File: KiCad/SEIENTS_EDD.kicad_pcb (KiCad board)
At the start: 2 copper layers, 130.1 x 90 mm, 99 parts, among them IC1 A3144EUA, J1 Conn_01x02_Pin, J201 Screw_Terminal_01x04, J3 Screw_Terminal_01x05, J4 Screw_Terminal_01x02, J7 DE9_Socket, J8 DE9_Pins, M4 Motor_DC, M5 Motor_DC, M6 Motor_DC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

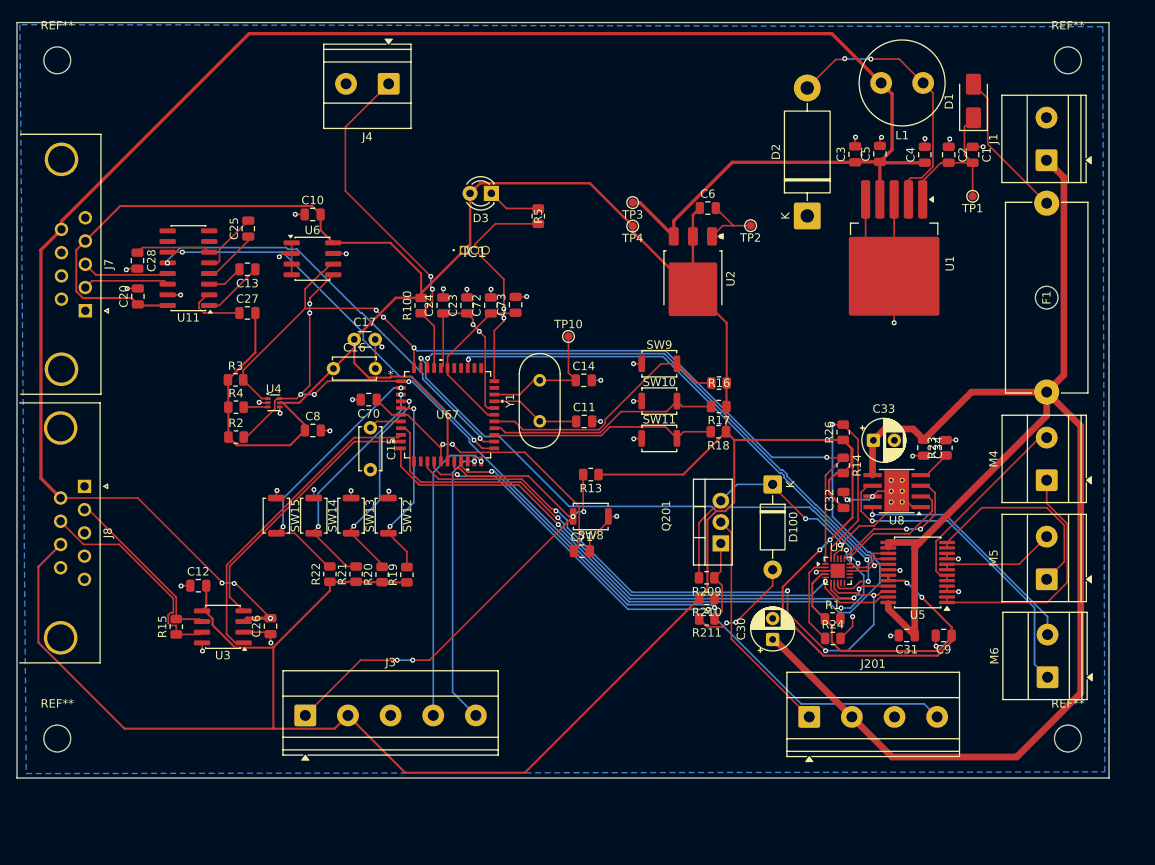
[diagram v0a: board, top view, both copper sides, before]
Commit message: Afegit el LTSpice
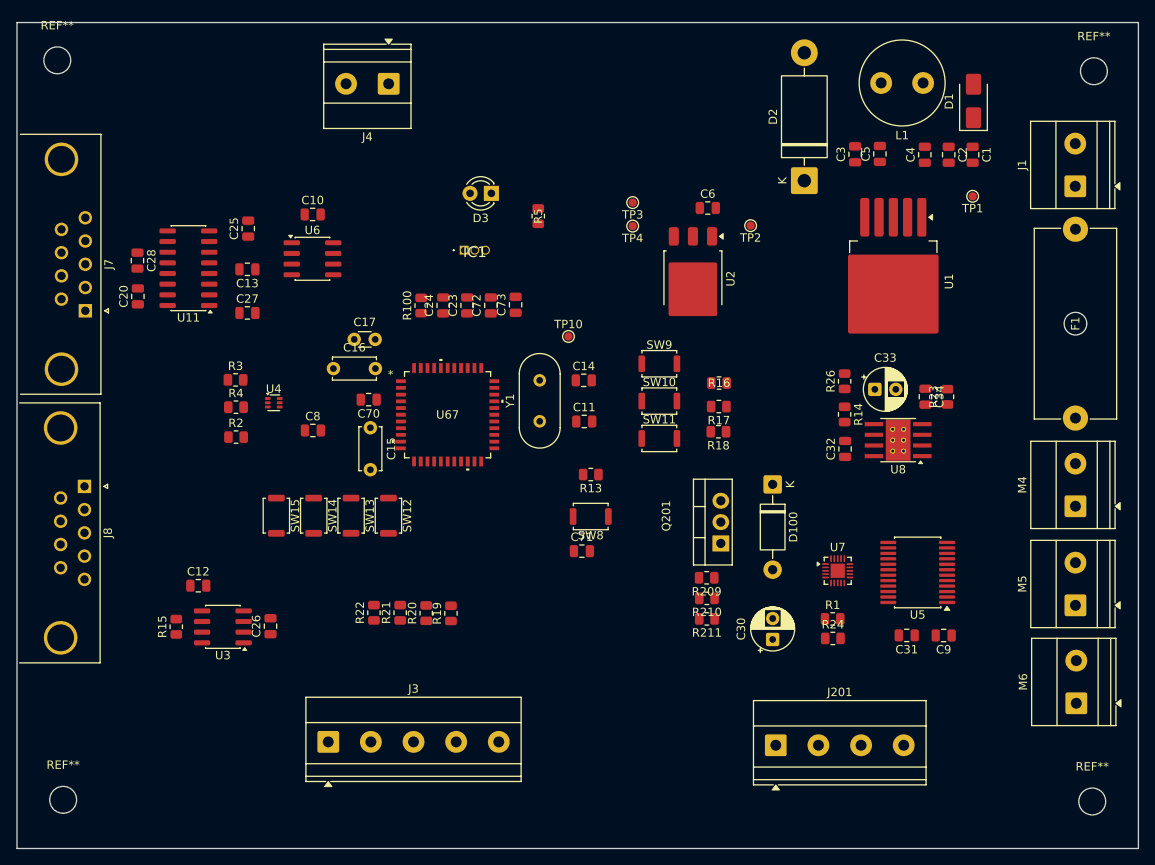
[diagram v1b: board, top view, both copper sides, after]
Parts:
- moved REF** 8.04 mm to (218.0, 147.8)
- moved REF** 7.33 mm to (95.4, 147.6)
- moved R19 6.98 mm to (141.6, 125.4)
- moved R22 6.98 mm to (132.4, 125.3)
- moved R20 6.98 mm to (138.7, 125.4)
- moved R21 6.98 mm to (135.6, 125.3)
- moved C32 6.08 mm to (188.6, 105.8)
- moved C34 6.08 mm to (198.1, 99.6)
- moved R14 6.08 mm to (188.5, 101.7)
- moved R26 6.08 mm to (188.5, 97.7)
- moved U8 6.08 mm to (194.9, 104.8)
- moved C33 6.08 mm to (192.1, 98.7)
- moved R23 6.08 mm to (200.8, 99.6)
- moved J201 5.22 mm to (180.3, 141.1)
- moved M5 4.62 mm to (216.0, 124.4)
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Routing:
- net +3.3V: track 519.9 -> 0.00 mm, vias 4 -> 0
- net +5V: track 235.2 -> 0.00 mm, vias 3 -> 0
- net VBAT: track 185.8 -> 0.00 mm
- net GND: track 153.2 -> 0.00 mm, vias 48 -> 0
- net MCU_SDA: track 148.8 -> 0.00 mm, vias 6 -> 0
- net MCU_SCL: track 109.7 -> 0.00 mm, vias 4 -> 0
- net POS_IN2: track 77.6 -> 0.00 mm, vias 4 -> 0
- net POS_PWM: track 72.3 -> 0.00 mm, vias 2 -> 0
- net POS_IN1: track 72.1 -> 0.00 mm, vias 3 -> 0
- net T_SEIENTS: track 71.5 -> 0.00 mm, vias 2 -> 0
- net REC_IN2: track 71.0 -> 0.00 mm, vias 2 -> 0
- net REC_IN1: track 70.5 -> 0.00 mm, vias 2 -> 0
- net REC_PWM: track 69.1 -> 0.00 mm, vias 3 -> 0
- net Net-(J3-Pin_1): track 65.0 -> 0.00 mm, vias 4 -> 0
- net CALEFACCIÓ: track 51.9 -> 0.00 mm, vias 2 -> 0
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- removed copper zone on B.Cu, net GND
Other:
- board size 130.1 x 90 mm -> 133.6 x 98.4 mm

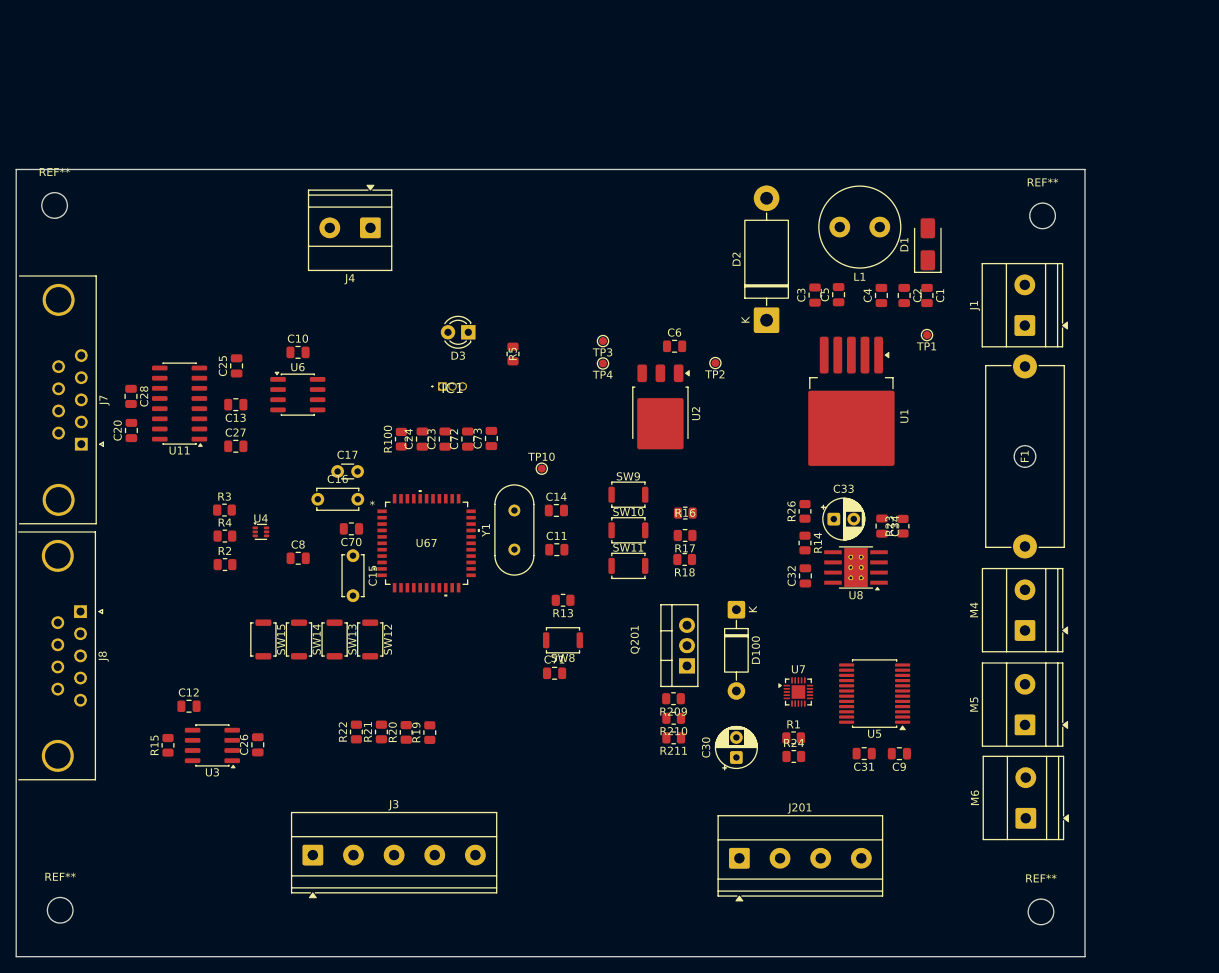
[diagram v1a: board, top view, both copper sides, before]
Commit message: Afegit el LTSpice
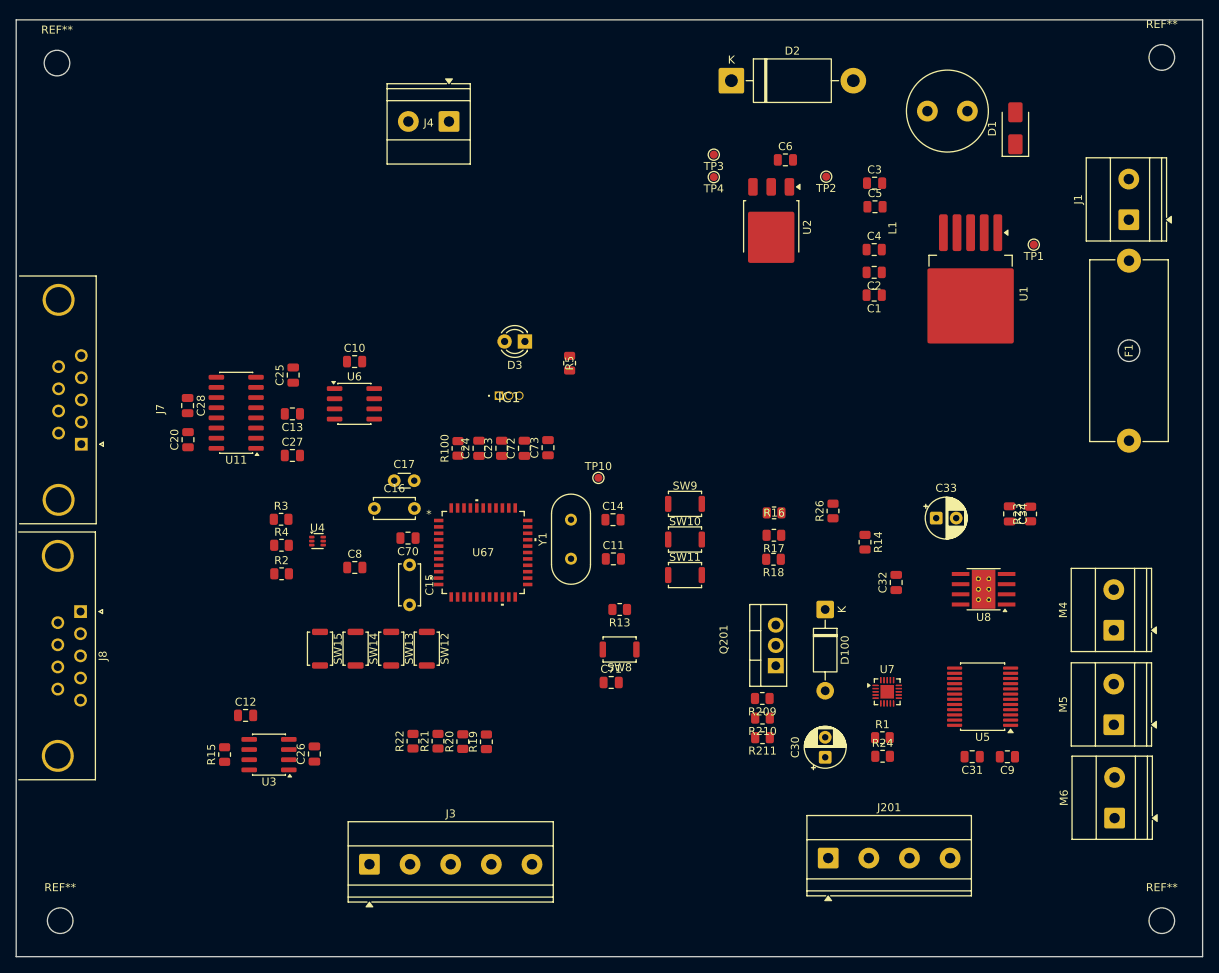
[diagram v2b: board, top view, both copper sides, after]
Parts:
- moved D2 30.3 mm to (179.3, 43.9), turned to 0 degrees
- moved C6 27.1 mm to (186.1, 53.8)
- moved TP2 27.1 mm to (191.2, 55.9)
- moved TP3 27.1 mm to (177.1, 53.1)
- moved TP4 27.1 mm to (177.1, 56.0)
- moved U2 27.1 mm to (184.3, 62.2)
- moved REF** 24.8 mm to (233.1, 41.0)
- moved U1 21.4 mm to (209.2, 70.5)
- moved F1 18.5 mm to (229.0, 88.9)
- moved J1 18.5 mm to (229.0, 61.3)
- moved L1 18.2 mm to (208.8, 47.7)
- moved D1 18.2 mm to (214.8, 49.9)
- moved REF** 17.8 mm to (95.0, 41.7)
- moved TP1 17.5 mm to (217.1, 64.4)
- moved J4 16.5 mm to (144.0, 49.0)
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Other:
- board size 133.6 x 98.4 mm -> 148.3 x 117.1 mm

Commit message: Modificació al placement
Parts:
- moved J1 109.0 mm to (124.0, 32.1)
- moved F1 107.6 mm to (137.5, 32.2), turned to 0 degrees
- moved C2 54.1 mm to (165.9, 23.6), turned to -90 degrees
- moved C1 53.3 mm to (172.5, 23.4), turned to -90 degrees
- moved TP1 48.7 mm to (175.3, 39.4)
- moved D1 47.6 mm to (170.6, 32.2), turned to 180 degrees
- moved U1 47.6 mm to (185.9, 29.1), turned to 90 degrees
- moved C6 47.6 mm to (224.0, 25.1), turned to -90 degrees
- moved C4 43.5 mm to (214.6, 25.1), turned to 90 degrees
- moved J3 43.4 mm to (177.2, 146.9)
- moved R5 41.6 mm to (130.1, 49.4)
- moved U2 40.5 mm to (216.9, 38.2)
- moved R18 38.1 mm to (156.0, 129.0), turned to 90 degrees
- moved IC1 36.6 mm to (138.1, 48.8), turned to 90 degrees
- moved C11 36.4 mm to (199.2, 92.5)
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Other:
- board size 148.3 x 117.1 mm -> 133.6 x 141.5 mm

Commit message: Modificació al placement
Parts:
- moved U6 114.7 mm to (46.9, 117.3)
- moved C10 114.0 mm to (47.2, 108.1)
- moved R22 99.2 mm to (170.5, 40.9), turned to 0 degrees
- moved SW15 96.7 mm to (177.2, 40.9), turned to 180 degrees
- moved R21 89.0 mm to (170.6, 48.5), turned to 0 degrees
- moved SW14 86.1 mm to (177.3, 48.6), turned to 180 degrees
- moved TP3 81.2 mm to (124.1, 28.1)
- moved C71 80.8 mm to (97.2, 89.3)
- moved R13 80.8 mm to (108.5, 89.3)
- moved SW8 80.8 mm to (103.3, 93.2)
- moved R20 79.2 mm to (170.6, 55.9), turned to 0 degrees
- moved C12 77.7 mm to (54.1, 86.8)
- moved C32 77.7 mm to (137.5, 92.3)
- moved C34 77.7 mm to (154.0, 86.5)
- moved C70 77.7 mm to (89.8, 89.3)
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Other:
- board size 133.6 x 141.5 mm -> 144.2 x 120.4 mm

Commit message: Modificació al placement
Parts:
- removed C30, C33: 10uF, Capacitor_THT:CP_Radial_D5.0mm_P2.50mm
- removed C31, C34, C9: 0.1uF, Capacitor_SMD:C_0805_2012Metric
- removed REF** (x4): MountingHole_3.2mm_M3, MountingHole:MountingHole_3.2mm_M3
- added C300: 0.1uF, Capacitor_SMD:C_0805_2012Metric, F.Cu at (43.8, 125.0)
- added C301: 10uF, Capacitor_THT:CP_Radial_D5.0mm_P2.50mm, F.Cu at (37.0, 126.8)
- added C302: 0.1uF, Capacitor_SMD:C_0805_2012Metric, F.Cu at (43.8, 128.0)
- added C303: 10uF, Capacitor_THT:CP_Radial_D5.0mm_P2.50mm, F.Cu at (37.0, 133.3)
- added C304: 0.1uF, Capacitor_SMD:C_0805_2012Metric, F.Cu at (43.8, 131.0)
- moved U5 109.9 mm to (40.9, 114.5)
- moved R23 100.2 mm to (60.2, 114.0)
- moved U8 100.2 mm to (54.4, 123.4)
- moved J201 100.0 mm to (66.3, 135.2), turned to 180 degrees
- moved D100 97.0 mm to (60.2, 164.8)
- moved R209 97.0 mm to (51.2, 152.2)
- moved R211 97.0 mm to (51.3, 157.1)
- moved Q201 97.0 mm to (54.0, 171.8)
- moved R1 97.0 mm to (67.3, 180.8)
- moved R14 97.0 mm to (62.9, 153.6)
- moved C32 97.0 mm to (66.8, 158.7)
- moved R210 97.0 mm to (51.3, 154.7)
- moved R24 97.0 mm to (67.4, 183.2)
- moved R26 97.0 mm to (58.9, 149.7)
- moved U7 97.0 mm to (68.0, 175.1)
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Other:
- board size 144.2 x 120.4 mm -> 147.1 x 122.2 mm

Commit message: Modificació al placement
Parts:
- moved C303 89.0 mm to (56.4, 46.5)
- moved C302 81.7 mm to (49.6, 46.5)
- moved C301 77.8 mm to (39.3, 49.0)
- moved C304 75.0 mm to (60.5, 57.9)
- moved C300 68.9 mm to (40.5, 56.1), turned to 90 degrees
- moved U5 58.4 mm to (49.5, 56.7)
- moved U8 36.9 mm to (45.4, 87.5)
- moved C10 32.0 mm to (148.7, 82.4)
- moved U6 32.0 mm to (148.5, 89.5)
- moved R23 26.7 mm to (55.6, 87.7), turned to -90 degrees
- moved C13 26.5 mm to (138.9, 65.9)
- moved C20 26.5 mm to (156.3, 65.4)
- moved C28 26.5 mm to (156.4, 72.6)
- moved C27 26.5 mm to (148.0, 59.2)
- moved C25 26.5 mm to (138.9, 71.0)
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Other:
- board size 147.1 x 122.2 mm -> 153.9 x 102.2 mm

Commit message: Modificació al placement
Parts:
- added REF**: MountingHole_2.1mm, MountingHole:MountingHole_2.1mm, F.Cu at (33.3, 26.1)
- added REF**: MountingHole_2.1mm, MountingHole:MountingHole_2.1mm, F.Cu at (179.7, 26.3)
- added REF**: MountingHole_2.1mm, MountingHole:MountingHole_2.1mm, F.Cu at (33.3, 128.8)
- added REF**: MountingHole_2.1mm, MountingHole:MountingHole_2.1mm, F.Cu at (179.7, 128.9)
- moved M4 178.2 mm to (37.4, 106.3), turned to -90 degrees
- moved M6 175.6 mm to (37.3, 82.8), turned to -90 degrees
- moved M5 175.2 mm to (37.4, 94.5), turned to -90 degrees
- moved R24 96.0 mm to (56.5, 87.8), turned to -90 degrees
- moved R1 95.3 mm to (73.3, 85.7), turned to 90 degrees
- moved C12 89.2 mm to (137.8, 88.6)
- moved R15 89.2 mm to (129.2, 94.7)
- moved U3 89.2 mm to (137.8, 94.6)
- moved U7 87.7 mm to (64.8, 87.5)
- moved C26 80.0 mm to (137.9, 104.4), turned to 0 degrees
- moved C32 77.9 mm to (56.5, 81.5)
- moved R14 62.7 mm to (73.2, 91.8)
- moved R211 62.4 mm to (85.2, 104.7), turned to 0 degrees
- moved D100 61.6 mm to (90.5, 111.2), turned to 180 degrees
- moved R22 61.3 mm to (177.2, 94.2), turned to 180 degrees
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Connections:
- C32 pad 2: GND -> +3.3V
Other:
- board size 153.9 x 102.2 mm -> 153.9 x 110 mm

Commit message: cambios en el placement
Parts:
- moved C5 71.1 mm to (70.9, 53.2), turned to -90 degrees
- moved C26 64.7 mm to (145.0, 40.0)
- moved R15 59.0 mm to (134.5, 35.9)
- moved U3 58.7 mm to (134.5, 35.9)
- moved C12 54.6 mm to (145.0, 34.5)
- moved D100 50.4 mm to (42.0, 124.9), turned to 0 degrees
- moved C1 48.8 mm to (58.9, 54.8)
- moved C4 47.5 mm to (93.1, 35.9)
- moved C11 45.5 mm to (78.9, 84.4)
- moved C3 42.5 mm to (88.0, 36.0)
- moved TP3 42.5 mm to (82.5, 37.0)
- moved C6 42.4 mm to (107.5, 35.0)
- moved TP1 42.3 mm to (58.8, 48.7)
- moved U1 42.3 mm to (69.4, 38.4)
- moved D1 42.3 mm to (54.1, 41.5)
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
